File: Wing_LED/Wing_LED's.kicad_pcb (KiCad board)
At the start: 2 copper layers, 50.8 x 22.9 mm, 42 parts, among them J1 feather long, J2 feather short

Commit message: Update_PCB
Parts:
- moved D15 1.13 mm to (139.8, 82.9)
- moved D12 1.07 mm to (157.4, 82.8)
- moved R12 1.03 mm to (139.8, 79.1)
- moved R16 1.00 mm to (157.3, 79.0)
- moved D13 0.76 mm to (160.8, 82.7)
- moved D11 0.66 mm to (164.2, 82.7)
- moved R17 0.64 mm to (160.8, 78.9)
- moved D19 0.52 mm to (171.4, 82.7)
- moved R18 0.52 mm to (164.1, 79.0)
- moved D10 0.51 mm to (167.8, 82.7)
- moved D16 0.49 mm to (143.8, 82.8)
- moved D18 0.49 mm to (150.7, 82.7)
- moved D17 0.48 mm to (147.1, 82.8)
- moved R20 0.33 mm to (171.3, 79.0)
- moved R19 0.30 mm to (167.8, 78.9)
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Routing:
- net /A0: track 4.13 -> 5.79 mm
- net /TX: track 4.40 -> 5.61 mm
- net /A1: track 3.93 -> 4.84 mm
- net /MISO: track 3.25 -> 3.91 mm
- net /D9: track 4.99 -> 5.60 mm
- net Net-(D16-Pad1): track 2.02 -> 1.46 mm
- net Net-(D12-Pad1): track 2.00 -> 1.45 mm
- net Net-(D11-Pad1): track 2.00 -> 1.46 mm
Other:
- net class Default removed
- board text added: "CIPO"
- board text added: "COPI"
- board text added: "D10"
- board text added: "D11"
- board text added: "D12"
- board text added: "D13"
- board text added: "D5"
- board text added: "D6"
- board text added: "D9"
- board text added: "NC"
- board text added: "VBUS"
- board text removed: "A4"
- board text removed: "A5"
- board text removed: "AREF"
- board text removed: "F0"
- board text removed: "F1"
- board text removed: "F2"
- board text removed: "F3"
- board text removed: "F4"
- board text removed: "F5"
- board text removed: "F6"
- board text removed: "FREE"
- board text removed: "MISO"
- board text removed: "MOSI"
- board text removed: "VBAT"
- board text removed: "VUSB"
- board text removed: "~RST"

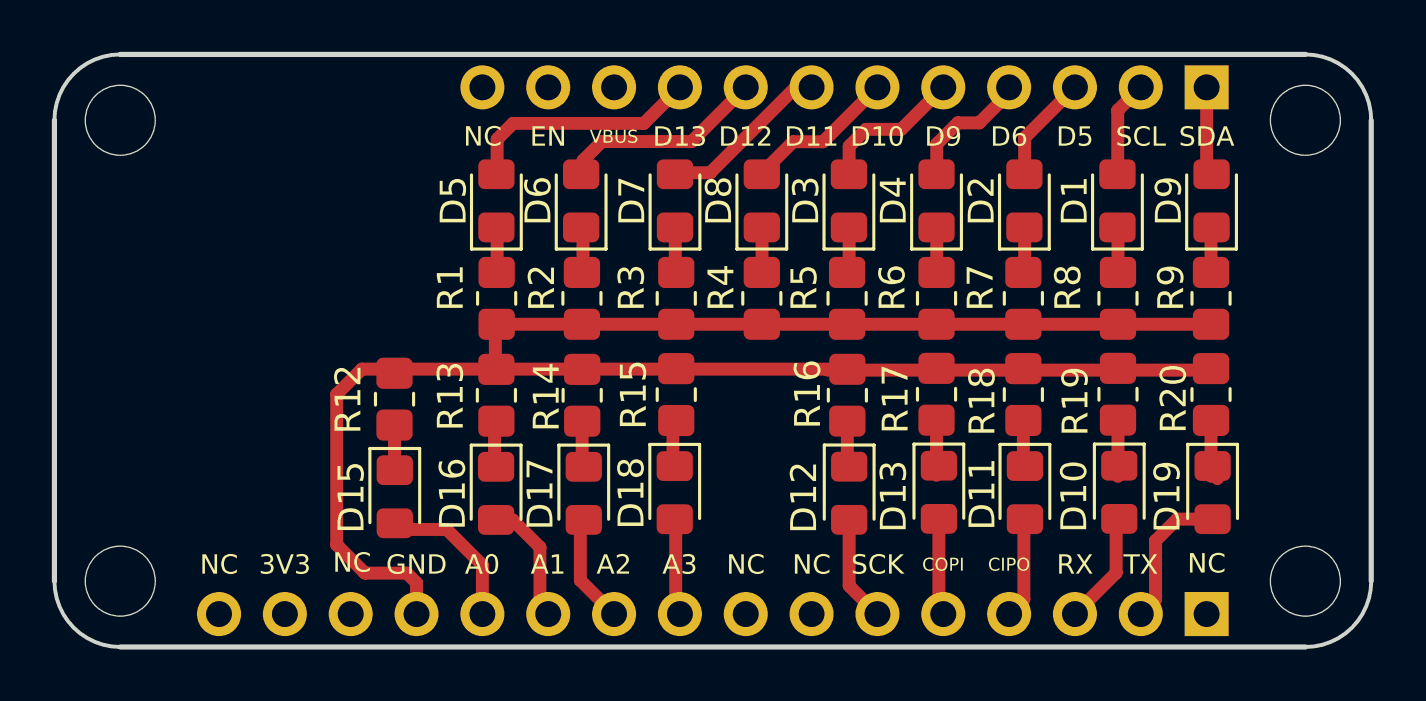
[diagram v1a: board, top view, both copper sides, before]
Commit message: Change_Labels
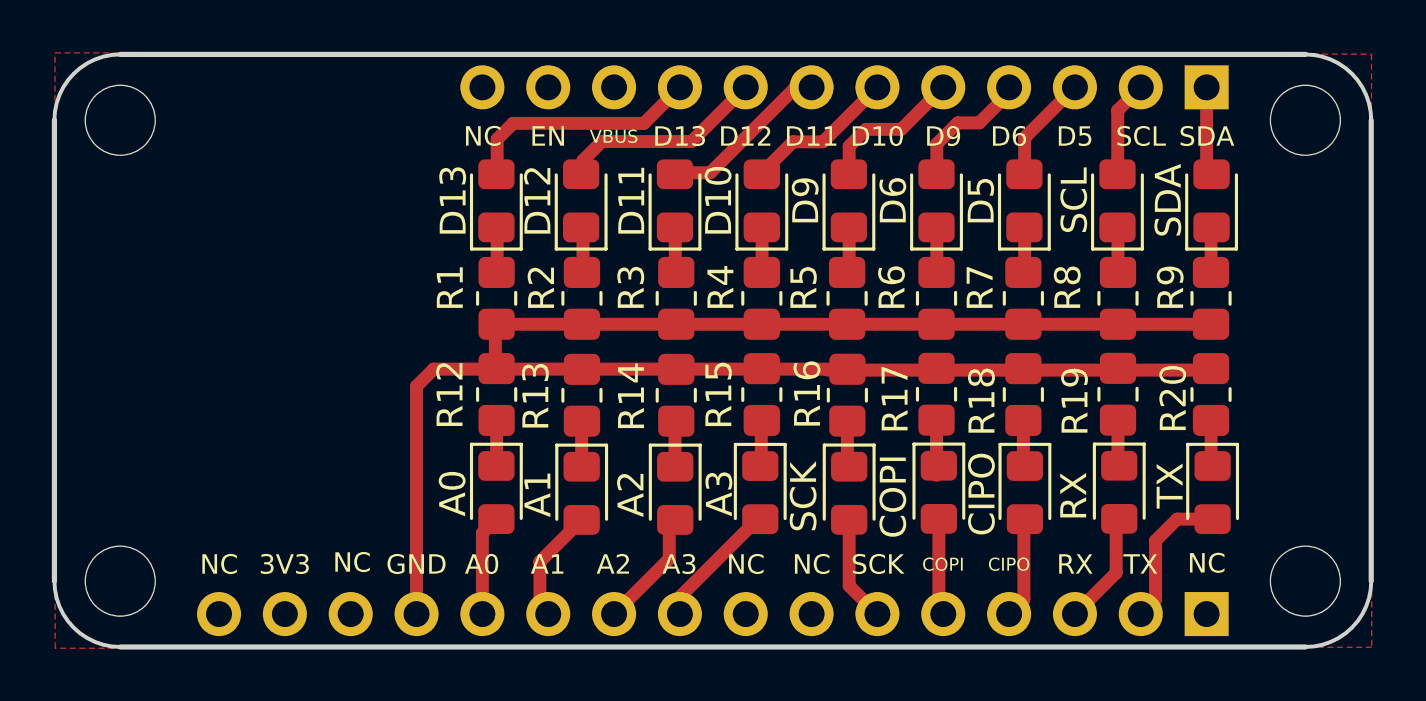
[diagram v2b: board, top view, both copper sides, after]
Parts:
- moved R12 3.94 mm to (143.8, 79.0)
- moved A0 3.92 mm to (143.8, 82.7)
- moved R14 3.63 mm to (150.7, 79.0)
- moved A2 3.53 mm to (150.7, 82.8)
- moved A1 3.30 mm to (147.1, 82.8)
- moved A3 3.30 mm to (153.9, 82.7)
- moved R13 3.30 mm to (147.1, 79.0)
- moved R15 3.30 mm to (154.0, 79.0)
- renumbered D15 to A0, D16 to A1, D17 to A2, D18 to A3, D11 to CIPO, D13 to COPI, D8 to D10, D7 to D11, D6 to D12, D5 to D13, D2 to D5, D4 to D6, D3 to D9, D10 to RX, D12 to SCK, D1 to SCL, D9 to SDA, D19 to TX
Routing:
- net GND: track 74.8 -> 69.6 mm
- net /A3: track 3.24 -> 5.23 mm
- net /A0: track 5.79 -> 3.89 mm
- net /A2: track 3.71 -> 4.51 mm
- added copper zone on F.Cu, net GND

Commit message: Add_Logo
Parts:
- added G***: LOGO, Aesthetics:electronic_cats_logo_4x3, F.Cu at (130.7, 76.8)
- added G***: LOGO, Aesthetics:electronic_cats_logo_4x3, B.Cu at (130.7, 76.7)
- added REF**: OSHW-Symbol_8.9x8mm_SilkScreen, Symbol:OSHW-Symbol_8.9x8mm_SilkScreen, B.Cu at (137.5, 77.0)
